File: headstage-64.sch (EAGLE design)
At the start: 183 parts, among them J8 DF40C-70DP-0.4V(51), U1 ADA4062-4ACPZ-R7, U10 BNO055, U11 TS4231, U12 TS4231, U13 TLV70733, U14 10M08DC, U15 TLV70733, U16 LT3463, U17 TLV70725, U18 TPS62621, U19 ASCO-50.000MHZ-EK-T3, U2 AD5681RBCPZ-1RL7, U20 TLV70712, U3 CAT4016_QFN, U4 TPL0501_UQFN, U5 DG509B, U6 TS4231, U7 RHD2064_BGA, U8 TS4231

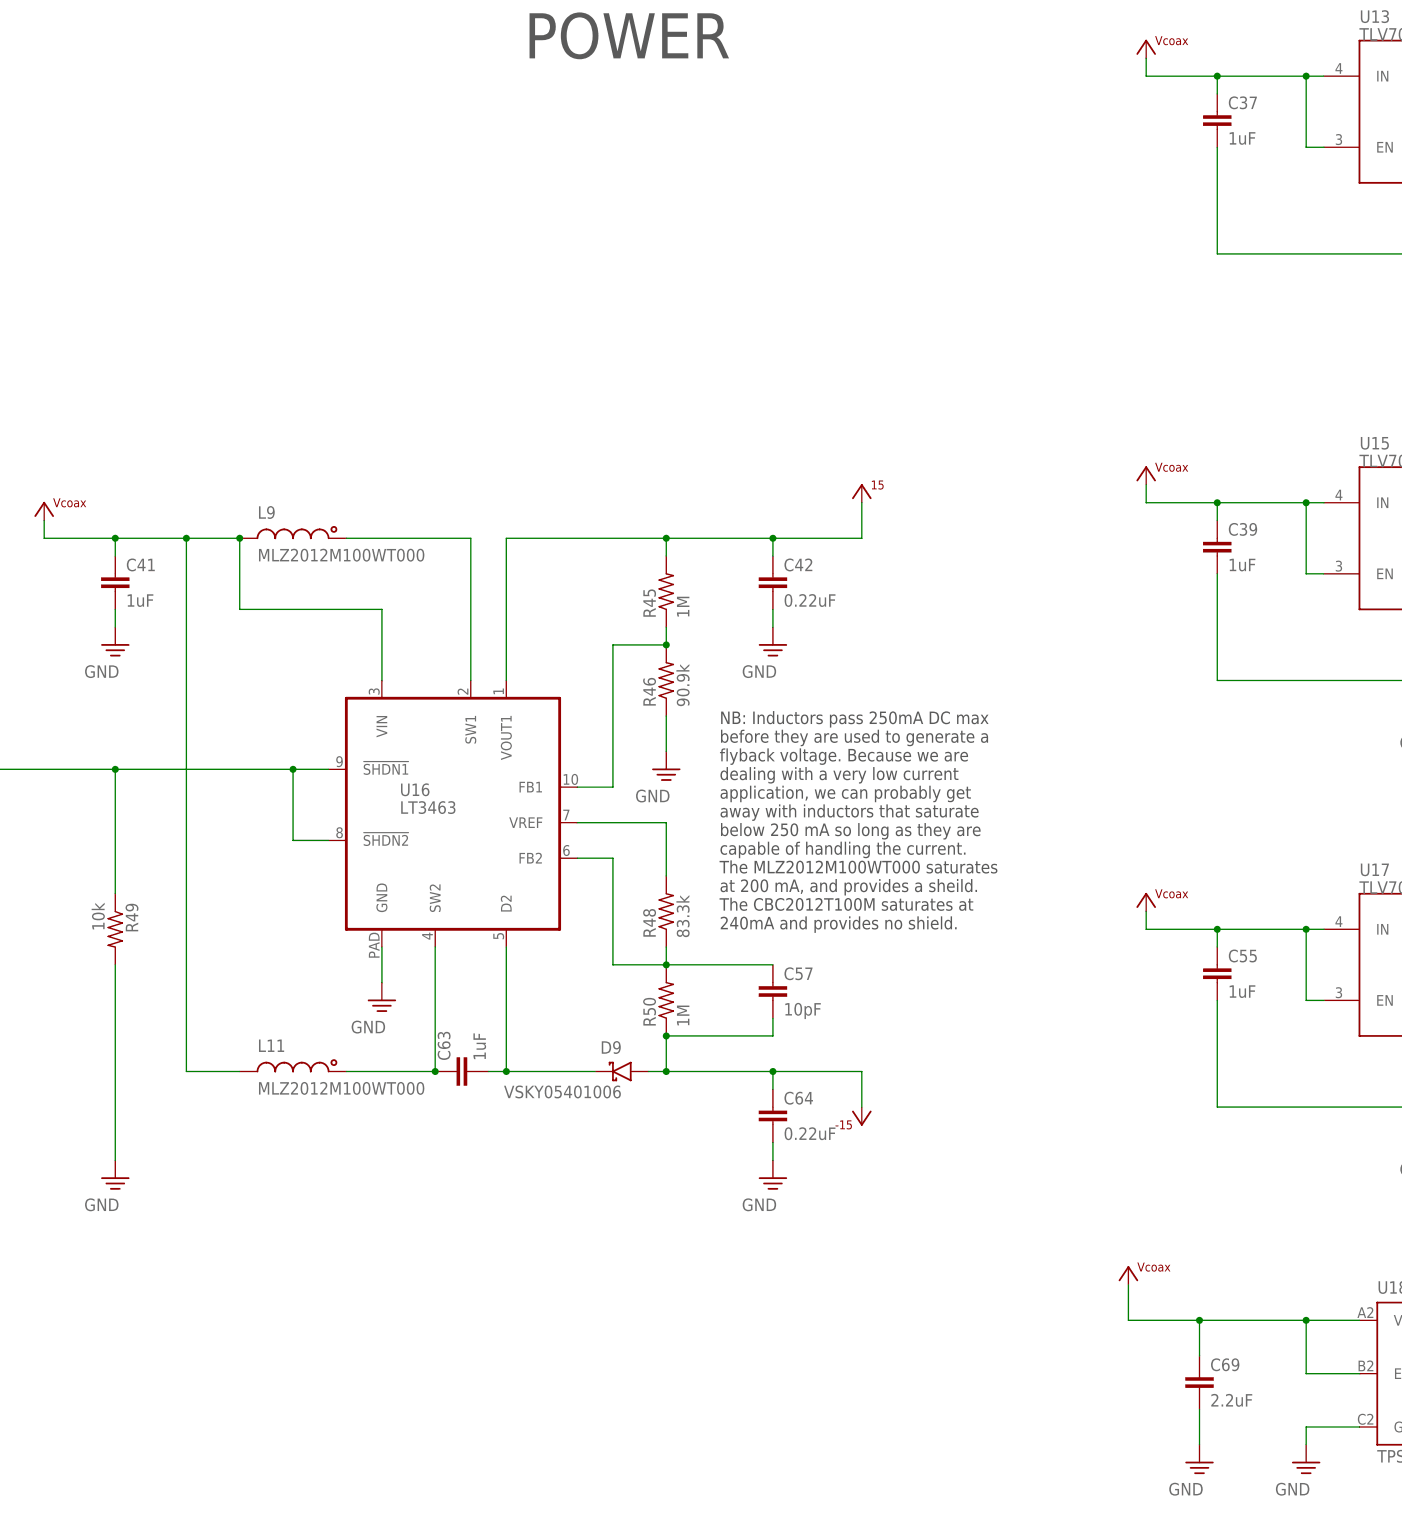
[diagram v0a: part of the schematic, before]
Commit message: Replace every bulk cap on Vcoax with 10uF
- To reduce near DC noise coming from power over coax and reduce BOM complexity
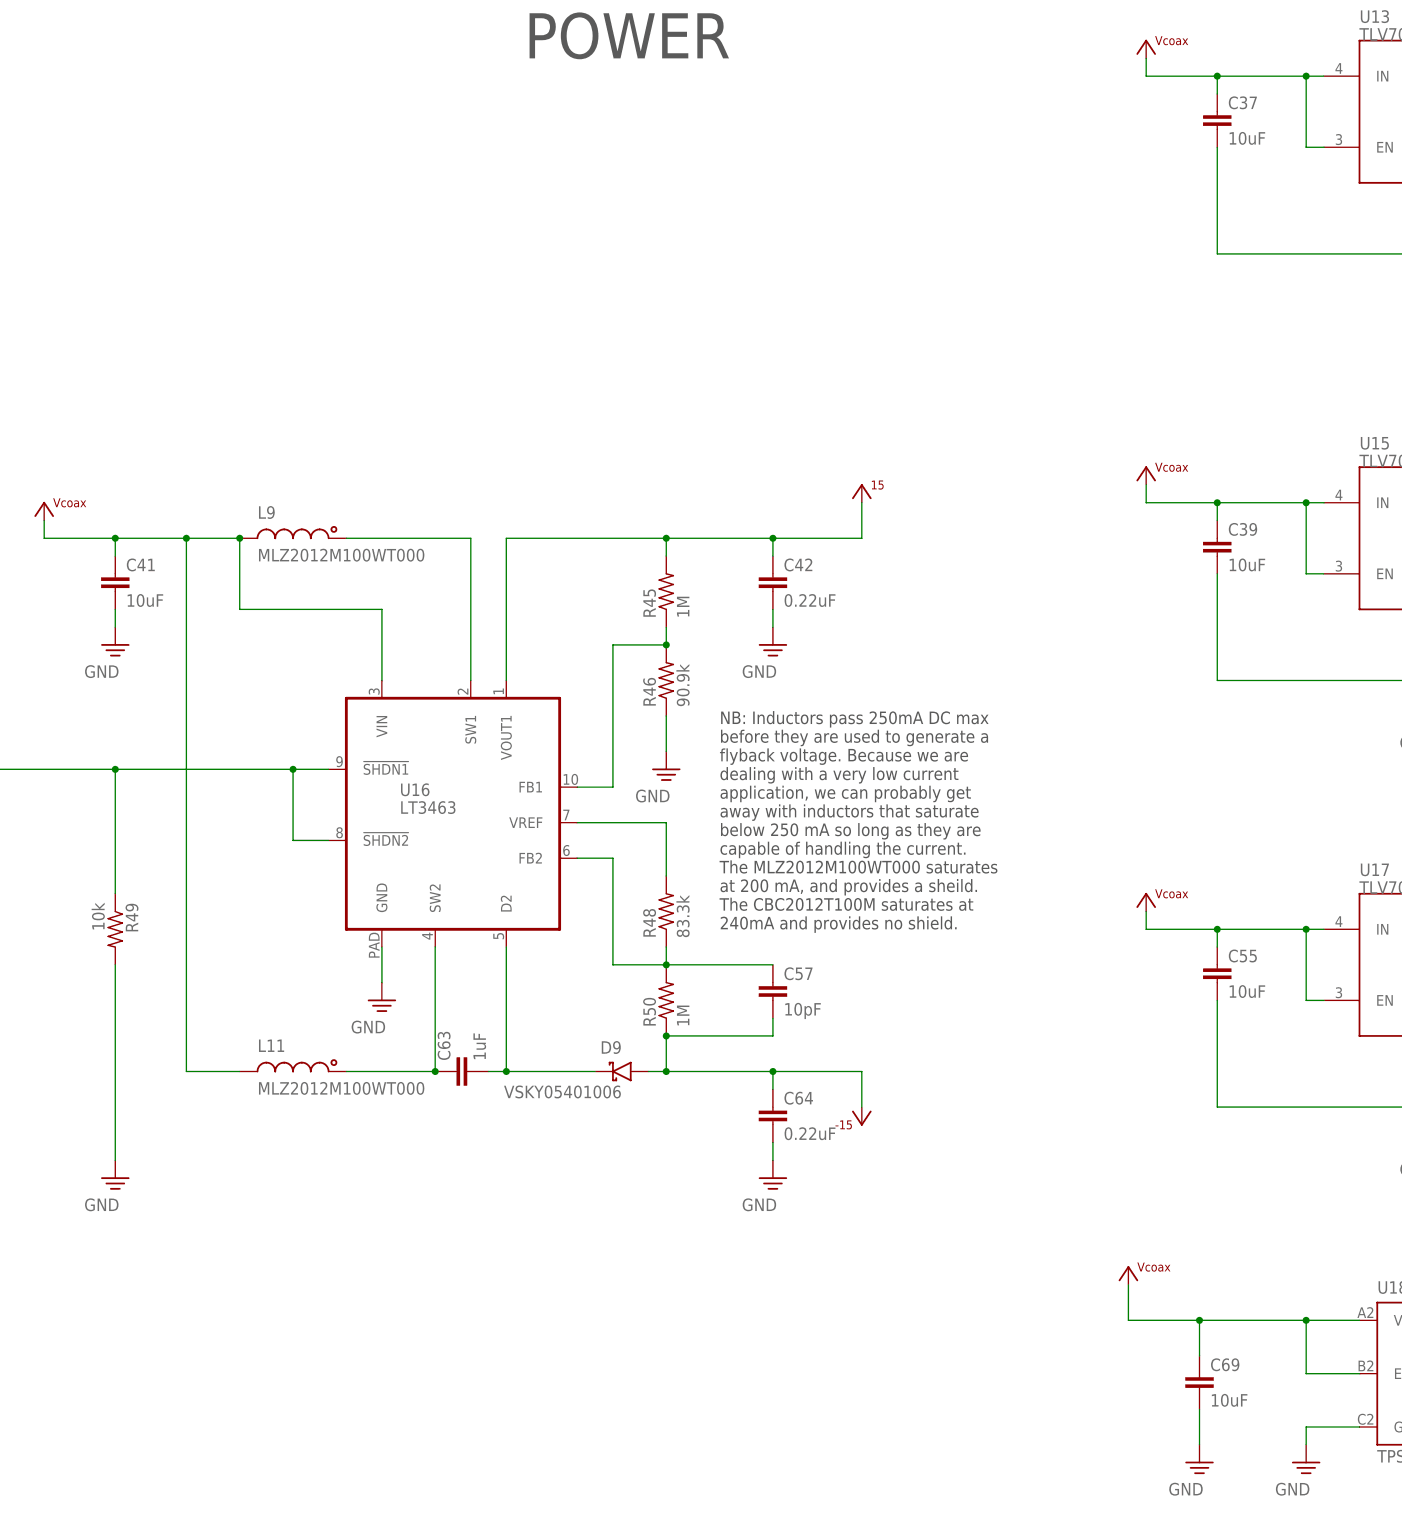
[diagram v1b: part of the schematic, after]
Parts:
- C37, C39, C41, C55: value 1uF -> 10uF
- C69: value 2.2uF -> 10uF
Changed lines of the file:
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@@
 <part name="C57" library="jonnew" deviceset="C" device="_0201T" value="10pF"/>
 <part name="SUPPLY26" library="jonnew" deviceset="GND" device=""/>
-<part name="C39" library="jonnew" deviceset="C" device="_0402T" value="1uF">
+<part name="C39" library="jonnew" deviceset="C" device="_0402T" value="10uF">
 <attribute name="PARTNO" value="CL05A105KO5NNNC"/>
 </part>
@@
 <attribute name="PARTNO" value="CL05A105KO5NNNC"/>
 </part>
-<part name="C55" library="jonnew" deviceset="C" device="_0402T" value="1uF">
-<attribute name="PARTNO" value="CL05A105KO5NNNC"/>
-</part>
-<part name="C41" library="jonnew" deviceset="C" device="_0402T" value="1uF">
+<part name="C55" library="jonnew" deviceset="C" device="_0402T" value="10uF">
+<attribute name="PARTNO" value="CL05A105KO5NNNC"/>
+</part>
+<part name="C41" library="jonnew" deviceset="C" device="_0402T" value="10uF">
 <attribute name="PARTNO" value="CL05A105KO5NNNC"/>
 </part>
@@
 <part name="SUPPLY66" library="jonnew" deviceset="AGND" device=""/>
 <part name="U13" library="jonnew" deviceset="TLV707" device="" value="TLV70733"/>
-<part name="C37" library="jonnew" deviceset="C" device="_0402T" value="1uF">
+<part name="C37" library="jonnew" deviceset="C" device="_0402T" value="10uF">
 <attribute name="PARTNO" value="CL05A105KO5NNNC"/>
 </part>
@@
 <part name="R44" library="jonnew" deviceset="R" device="_0201T" value="4.7k"/>
 <part name="U18" library="jonnew" deviceset="TPS6262X" device="" value="TPS62621"/>
-<part name="C69" library="jonnew" deviceset="C" device="_0402T" value="2.2uF">
-<attribute name="PARTNO" value="CL05A105KO5NNNC"/>
-</part>
+<part name="C69" library="jonnew" deviceset="C" device="_0402T" value="10uF">
+<attribute name="PARTNO" value="CL05A105KO5NNNC"/>
+</part>

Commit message: 22uF caps replaced with 15uF due to ease of sourcing.
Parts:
- C24, C73: value 22uF -> 15uF
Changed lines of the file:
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@@
 <part name="R25" library="jonnew" deviceset="R" device="_0201T" value="49.9"/>
 <part name="SUPPLY35" library="jonnew" deviceset="GND" device=""/>
-<part name="C24" library="jonnew" deviceset="C" device="_0402T" value="22uF">
+<part name="C24" library="jonnew" deviceset="C" device="_0402T" value="15uF">
 <attribute name="PARTNO" value="CL05A226MQ5QUNC"/>
 </part>
@@
 <attribute name="PARTNO" value="CL03A105MP3ZSNH"/>
 </part>
-<part name="C73" library="jonnew" deviceset="C" device="_0402T" value="22uF">
+<part name="C73" library="jonnew" deviceset="C" device="_0402T" value="15uF">
 <attribute name="PARTNO" value="CL05A226MQ6ZUN8"/>
 </part>
